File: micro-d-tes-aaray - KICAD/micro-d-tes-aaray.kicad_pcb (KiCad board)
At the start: 4 copper layers, 35.5 x 63.5 mm, 56 parts, among them J1 Conn_01x01_Socket, J10 Conn_01x01_Socket, J11 Conn_01x01_Socket, J12 Conn_01x01_Socket, J13 Conn_01x01_Socket, J14 Conn_01x01_Socket, J15 Conn_01x01_Socket, J16 Conn_01x01_Socket, J17 Conn_01x01_Socket, J18 Conn_01x01_Socket, J19 Conn_01x01_Socket, J2 Conn_01x01_Socket, J20 Conn_01x01_Socket, J21 Conn_01x01_Socket, J22 Conn_01x01_Socket, J23 Conn_01x01_Socket, J24 Conn_01x01_Socket, J25 Conn_01x01_Socket, J26 DB25_Plug, J3 Conn_01x01_Socket, J4 Conn_01x01_Socket, J5 Conn_01x01_Socket, J6 Conn_01x01_Socket, J7 Conn_01x01_Socket, J8 Conn_01x01_Socket, J9 Conn_01x01_Socket, J99 DB25_Plug

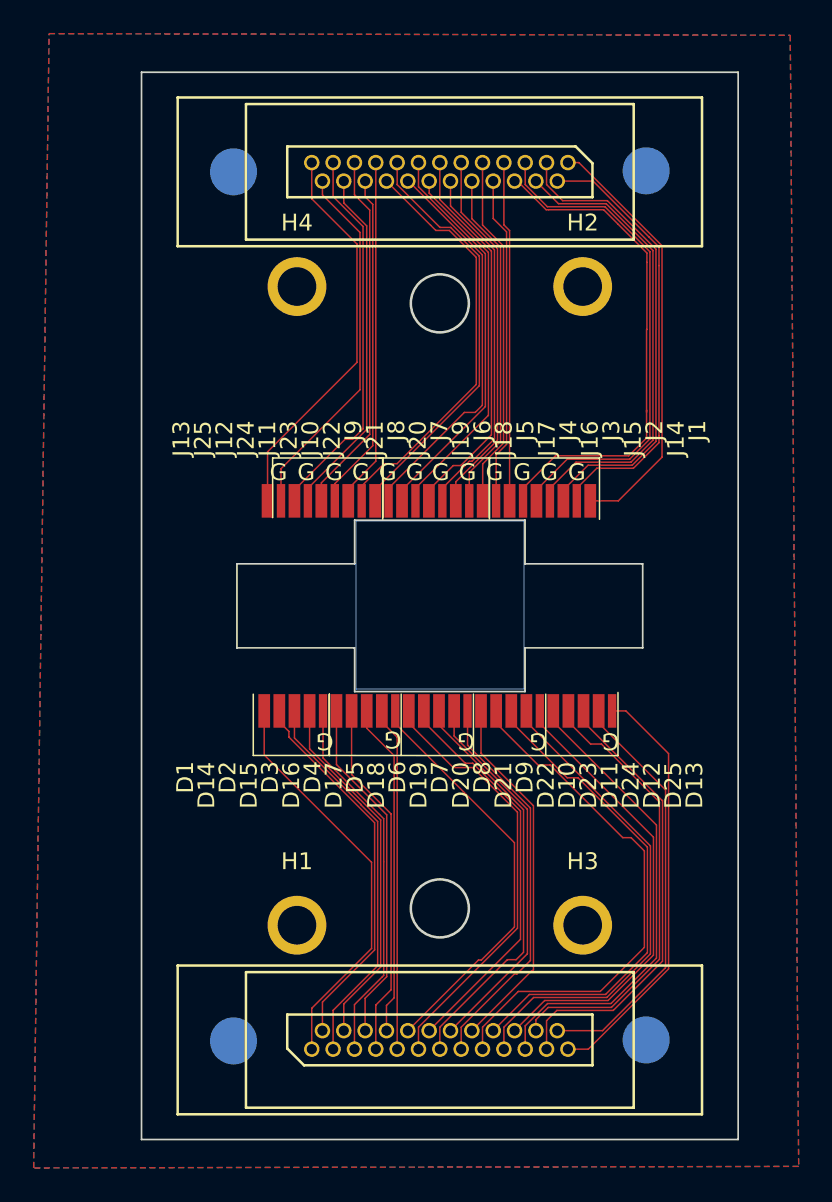
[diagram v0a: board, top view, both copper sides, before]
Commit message: fixed 8-32s
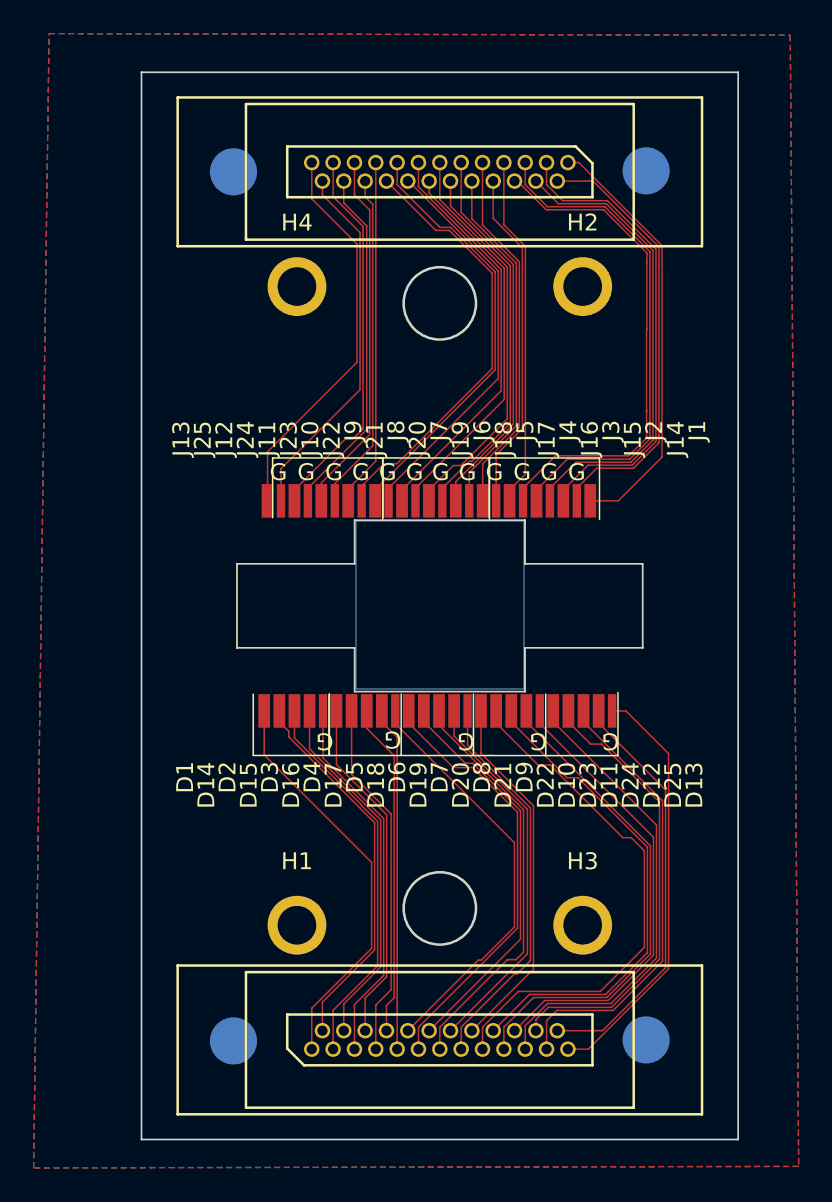
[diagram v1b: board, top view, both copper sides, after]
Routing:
- net Net-(J22-Pin_1): track 25.0 -> 25.8 mm
- net Net-(J9-Pin_1): track 25.1 -> 25.9 mm
- net Net-(J8-Pin_1): track 23.8 -> 24.6 mm
- net Net-(J19-Pin_1): track 21.5 -> 22.3 mm
- net Net-(J7-Pin_1): track 23.2 -> 24.0 mm
- net Net-(J6-Pin_1): track 22.0 -> 22.8 mm
- net Net-(J5-Pin_1): track 21.2 -> 21.9 mm
- net Net-(J18-Pin_1): track 20.5 -> 21.3 mm
- net Net-(J17-Pin_1): track 19.6 -> 20.4 mm
- net Net-(J4-Pin_1): track 20.3 -> 21.0 mm
- net Net-(J20-Pin_1): track 22.3 -> 23.1 mm
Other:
- outline, holes or cut-outs redrawn

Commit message: update
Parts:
- 1: renamed from J1; footprint 0_footprint_Library:SolderWirePad_1x01_SMD_0.7x2mm -> 0_footprint_Library:SolderWirePad_1x01_SMD_0.258x2mm
- 1: renamed from D1; footprint 0_footprint_Library:SolderWirePad_1x01_SMD_0.7x2mm -> 0_footprint_Library:SolderWirePad_1x01_SMD_0.258x2mm
- 10: renamed from D10; footprint 0_footprint_Library:SolderWirePad_1x01_SMD_0.7x2mm -> 0_footprint_Library:SolderWirePad_1x01_SMD_0.258x2mm
- 10: renamed from J10; footprint 0_footprint_Library:SolderWirePad_1x01_SMD_0.7x2mm -> 0_footprint_Library:SolderWirePad_1x01_SMD_0.258x2mm
- 11: renamed from D11; footprint 0_footprint_Library:SolderWirePad_1x01_SMD_0.7x2mm -> 0_footprint_Library:SolderWirePad_1x01_SMD_0.258x2mm
- 11: renamed from J11; footprint 0_footprint_Library:SolderWirePad_1x01_SMD_0.7x2mm -> 0_footprint_Library:SolderWirePad_1x01_SMD_0.258x2mm
- 12: renamed from J13; footprint 0_footprint_Library:SolderWirePad_1x01_SMD_0.7x2mm -> 0_footprint_Library:SolderWirePad_1x01_SMD_0.258x2mm
- 12: renamed from D12; footprint 0_footprint_Library:SolderWirePad_1x01_SMD_0.7x2mm -> 0_footprint_Library:SolderWirePad_1x01_SMD_0.258x2mm
- 12: renamed from J12; footprint 0_footprint_Library:SolderWirePad_1x01_SMD_0.7x2mm -> 0_footprint_Library:SolderWirePad_1x01_SMD_0.258x2mm
- 14: renamed from D14; footprint 0_footprint_Library:SolderWirePad_1x01_SMD_0.7x2mm -> 0_footprint_Library:SolderWirePad_1x01_SMD_0.258x2mm
- 15: renamed from D15; footprint 0_footprint_Library:SolderWirePad_1x01_SMD_0.7x2mm -> 0_footprint_Library:SolderWirePad_1x01_SMD_0.258x2mm
- 16: renamed from D16; footprint 0_footprint_Library:SolderWirePad_1x01_SMD_0.7x2mm -> 0_footprint_Library:SolderWirePad_1x01_SMD_0.258x2mm
- 17: renamed from D17; footprint 0_footprint_Library:SolderWirePad_1x01_SMD_0.7x2mm -> 0_footprint_Library:SolderWirePad_1x01_SMD_0.258x2mm
- 19: renamed from D19; footprint 0_footprint_Library:SolderWirePad_1x01_SMD_0.7x2mm -> 0_footprint_Library:SolderWirePad_1x01_SMD_0.258x2mm
- 2: renamed from D2; footprint 0_footprint_Library:SolderWirePad_1x01_SMD_0.7x2mm -> 0_footprint_Library:SolderWirePad_1x01_SMD_0.258x2mm
- 2: renamed from J2; footprint 0_footprint_Library:SolderWirePad_1x01_SMD_0.7x2mm -> 0_footprint_Library:SolderWirePad_1x01_SMD_0.258x2mm
- 20: renamed from D20; footprint 0_footprint_Library:SolderWirePad_1x01_SMD_0.7x2mm -> 0_footprint_Library:SolderWirePad_1x01_SMD_0.258x2mm
- 21: renamed from D21; footprint 0_footprint_Library:SolderWirePad_1x01_SMD_0.7x2mm -> 0_footprint_Library:SolderWirePad_1x01_SMD_0.258x2mm
- 22: renamed from D22; footprint 0_footprint_Library:SolderWirePad_1x01_SMD_0.7x2mm -> 0_footprint_Library:SolderWirePad_1x01_SMD_0.258x2mm
- 24: renamed from D24; footprint 0_footprint_Library:SolderWirePad_1x01_SMD_0.7x2mm -> 0_footprint_Library:SolderWirePad_1x01_SMD_0.258x2mm
- 25: renamed from D25; footprint 0_footprint_Library:SolderWirePad_1x01_SMD_0.7x2mm -> 0_footprint_Library:SolderWirePad_1x01_SMD_0.258x2mm
- 3: renamed from J3; footprint 0_footprint_Library:SolderWirePad_1x01_SMD_0.7x2mm -> 0_footprint_Library:SolderWirePad_1x01_SMD_0.258x2mm
- 4: renamed from D4; footprint 0_footprint_Library:SolderWirePad_1x01_SMD_0.7x2mm -> 0_footprint_Library:SolderWirePad_1x01_SMD_0.258x2mm
- 4: renamed from J4; footprint 0_footprint_Library:SolderWirePad_1x01_SMD_0.7x2mm -> 0_footprint_Library:SolderWirePad_1x01_SMD_0.258x2mm
- 5: renamed from J5; footprint 0_footprint_Library:SolderWirePad_1x01_SMD_0.7x2mm -> 0_footprint_Library:SolderWirePad_1x01_SMD_0.258x2mm
- 5: renamed from D5; footprint 0_footprint_Library:SolderWirePad_1x01_SMD_0.7x2mm -> 0_footprint_Library:SolderWirePad_1x01_SMD_0.258x2mm
- 6: renamed from D6; footprint 0_footprint_Library:SolderWirePad_1x01_SMD_0.7x2mm -> 0_footprint_Library:SolderWirePad_1x01_SMD_0.258x2mm
- 6: renamed from J6; footprint 0_footprint_Library:SolderWirePad_1x01_SMD_0.7x2mm -> 0_footprint_Library:SolderWirePad_1x01_SMD_0.258x2mm
- 7: renamed from J7; footprint 0_footprint_Library:SolderWirePad_1x01_SMD_0.7x2mm -> 0_footprint_Library:SolderWirePad_1x01_SMD_0.258x2mm
- 7: renamed from D7; footprint 0_footprint_Library:SolderWirePad_1x01_SMD_0.7x2mm -> 0_footprint_Library:SolderWirePad_1x01_SMD_0.258x2mm
- 8: renamed from J8; footprint 0_footprint_Library:SolderWirePad_1x01_SMD_0.7x2mm -> 0_footprint_Library:SolderWirePad_1x01_SMD_0.258x2mm
- 9: renamed from J9; footprint 0_footprint_Library:SolderWirePad_1x01_SMD_0.7x2mm -> 0_footprint_Library:SolderWirePad_1x01_SMD_0.258x2mm
- 9: renamed from D9; footprint 0_footprint_Library:SolderWirePad_1x01_SMD_0.7x2mm -> 0_footprint_Library:SolderWirePad_1x01_SMD_0.258x2mm
- moved 1 3.17 mm to (7.30, 41.2)
- moved 10 3.17 mm to (22.9, 41.2)
- moved 11 3.17 mm to (24.5, 41.2)
- moved 12 3.17 mm to (26.3, 41.2)
- moved 14 3.17 mm to (8.20, 41.2)
- moved 15 3.17 mm to (10.0, 41.2)
- moved 16 3.17 mm to (11.6, 41.2)
- moved 17 3.17 mm to (13.4, 41.2)
- moved 18 3.17 mm to (15.1, 41.2)
- moved 19 3.17 mm to (16.8, 41.2)
- moved 2 3.17 mm to (9.10, 41.2)
- moved 20 3.17 mm to (18.6, 41.2)
- moved 21 3.17 mm to (20.2, 41.2)
- moved 22 3.17 mm to (22.0, 41.2)
- moved 23 3.17 mm to (23.7, 41.2)
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- renumbered J14 to 14, J15 to 15, J16 to 16, J17 to 17, J18 to 18, D18 to 18, J19 to 19, J20 to 20, J21 to 21, J22 to 22, J23 to 23, D23 to 23, J24 to 24, J25 to 25, D3 to 3, D8 to 8
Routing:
- net Net-(J16-Pin_1): track 30.1 -> 15.9 mm, vias 0 -> 1
- net Net-(D22-Pin_1): track 29.2 -> 15.5 mm, vias 0 -> 1
- net Net-(J3-Pin_1): track 30.2 -> 17.4 mm, vias 0 -> 1
- net Net-(D10-Pin_1): track 29.3 -> 16.7 mm, vias 0 -> 1
- net Net-(D23-Pin_1): track 27.5 -> 16.1 mm, vias 0 -> 1
- net Net-(J15-Pin_1): track 28.0 -> 16.7 mm, vias 0 -> 1
- net Net-(D11-Pin_1): track 28.1 -> 17.6 mm, vias 0 -> 1
- net Net-(D24-Pin_1): track 26.9 -> 16.9 mm, vias 0 -> 1
- net Net-(J2-Pin_1): track 28.2 -> 18.3 mm, vias 0 -> 1
- net Net-(J10-Pin_1): track 20.8 -> 30.4 mm, vias 0 -> 1
- net Net-(D9-Pin_1): track 31.3 -> 22.6 mm, vias 0 -> 1
- net Net-(J14-Pin_1): track 26.1 -> 17.6 mm, vias 0 -> 1
- net Net-(D12-Pin_1): track 26.9 -> 18.6 mm, vias 0 -> 1
- net Net-(J21-Pin_1): track 24.0 -> 32.0 mm, vias 0 -> 1
- net Net-(J23-Pin_1): track 20.2 -> 28.2 mm, vias 0 -> 1
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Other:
- outline, holes or cut-outs redrawn
